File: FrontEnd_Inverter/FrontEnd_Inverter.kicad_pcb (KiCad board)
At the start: 4 copper layers, 210 x 127 mm, 75 parts, among them J1 Conn_02x20_Odd_Even, J11 CONN_02X06, P0 CONN_01X03, P10 CONN_01X02, P11 CONN_01X03, P20 CONN_01X02, P7 CONN_01X03, T1 SKiiP_13ACM12V18, U11 ACS758xCB-PFF, U12 ACS758xCB-PFF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

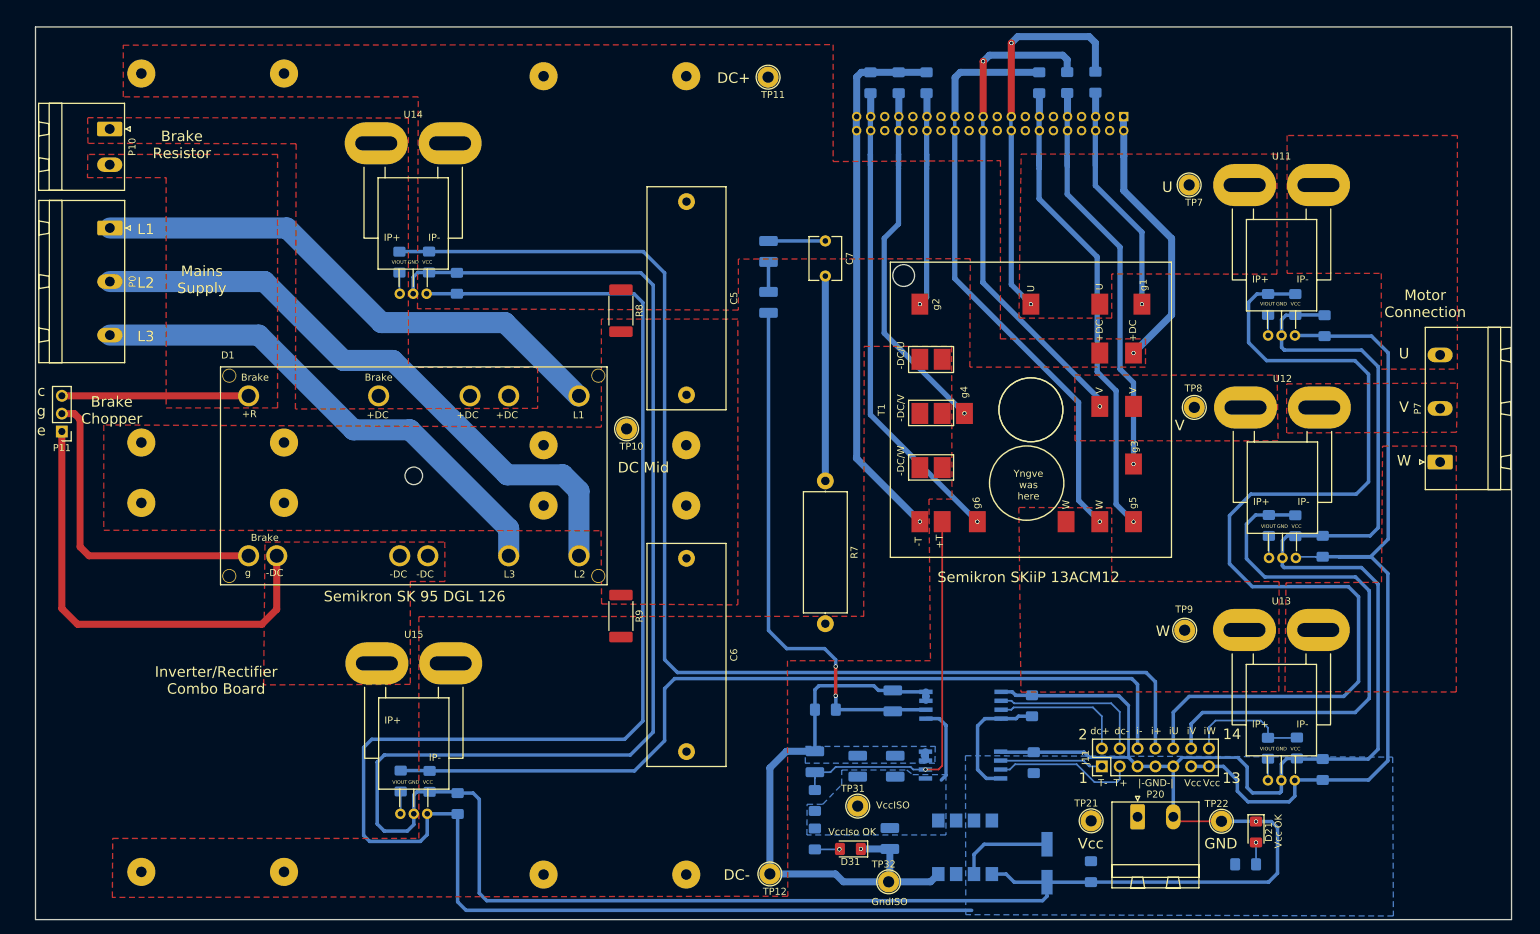
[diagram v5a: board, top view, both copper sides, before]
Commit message: Tweaking position of snubber components C7 and R7 to get closer to DC+ at inverter module T1. Work in progress.
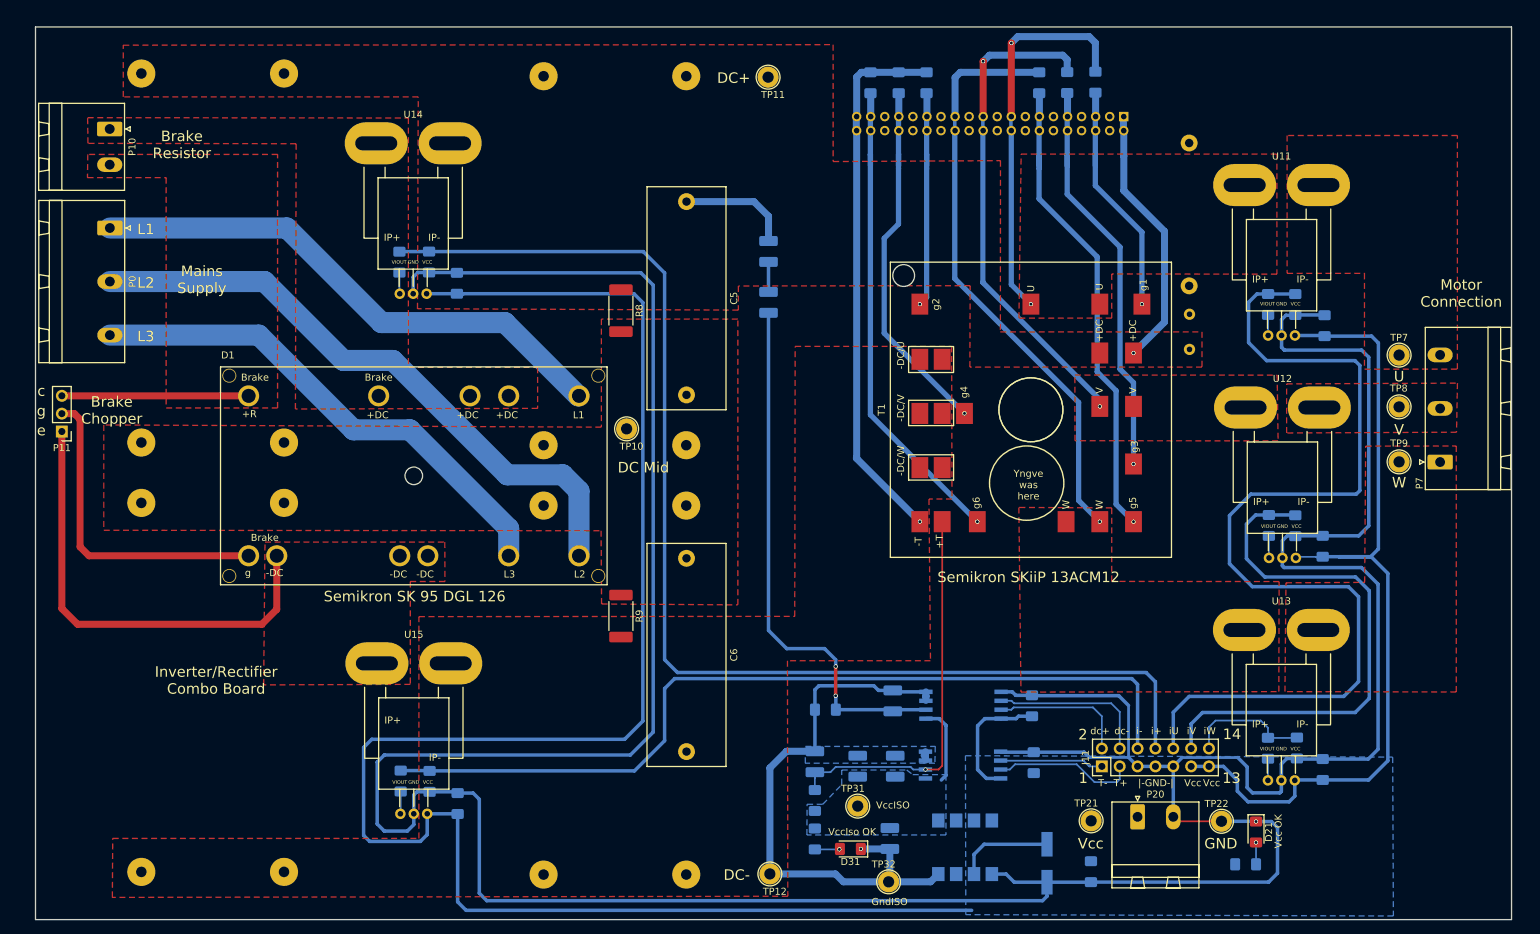
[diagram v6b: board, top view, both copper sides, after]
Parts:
- C7, R7: moved to B.Cu
- moved R7 58.7 mm to (202.1, 52.8), turned to 90 degrees
- moved C7 54.1 mm to (202.2, 61.9), turned to 90 degrees
- moved TP9 38.8 mm to (232.0, 77.9)
- moved TP7 38.4 mm to (232.0, 62.7)
- moved TP8 29.1 mm to (232.0, 70.1)
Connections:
- TP7 pad 1: U -> Net-(P7-Pad3)
- TP8 pad 1: V -> Net-(P7-Pad2)
- TP9 pad 1: W -> Net-(P7-Pad1)
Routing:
- net Net-(C7-Pad2): track 29.1 -> 0.00 mm
- net DC+: track 46.8 -> 53.9 mm
- net GND: track 532.6 -> 530.5 mm
- net VCC: track 404.0 -> 402.8 mm
- net Net-(C20-Pad1): track 141.5 -> 140.4 mm

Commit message: Finalized C7 and R7 placement. Started improving gatedriver connection with zones and vias.
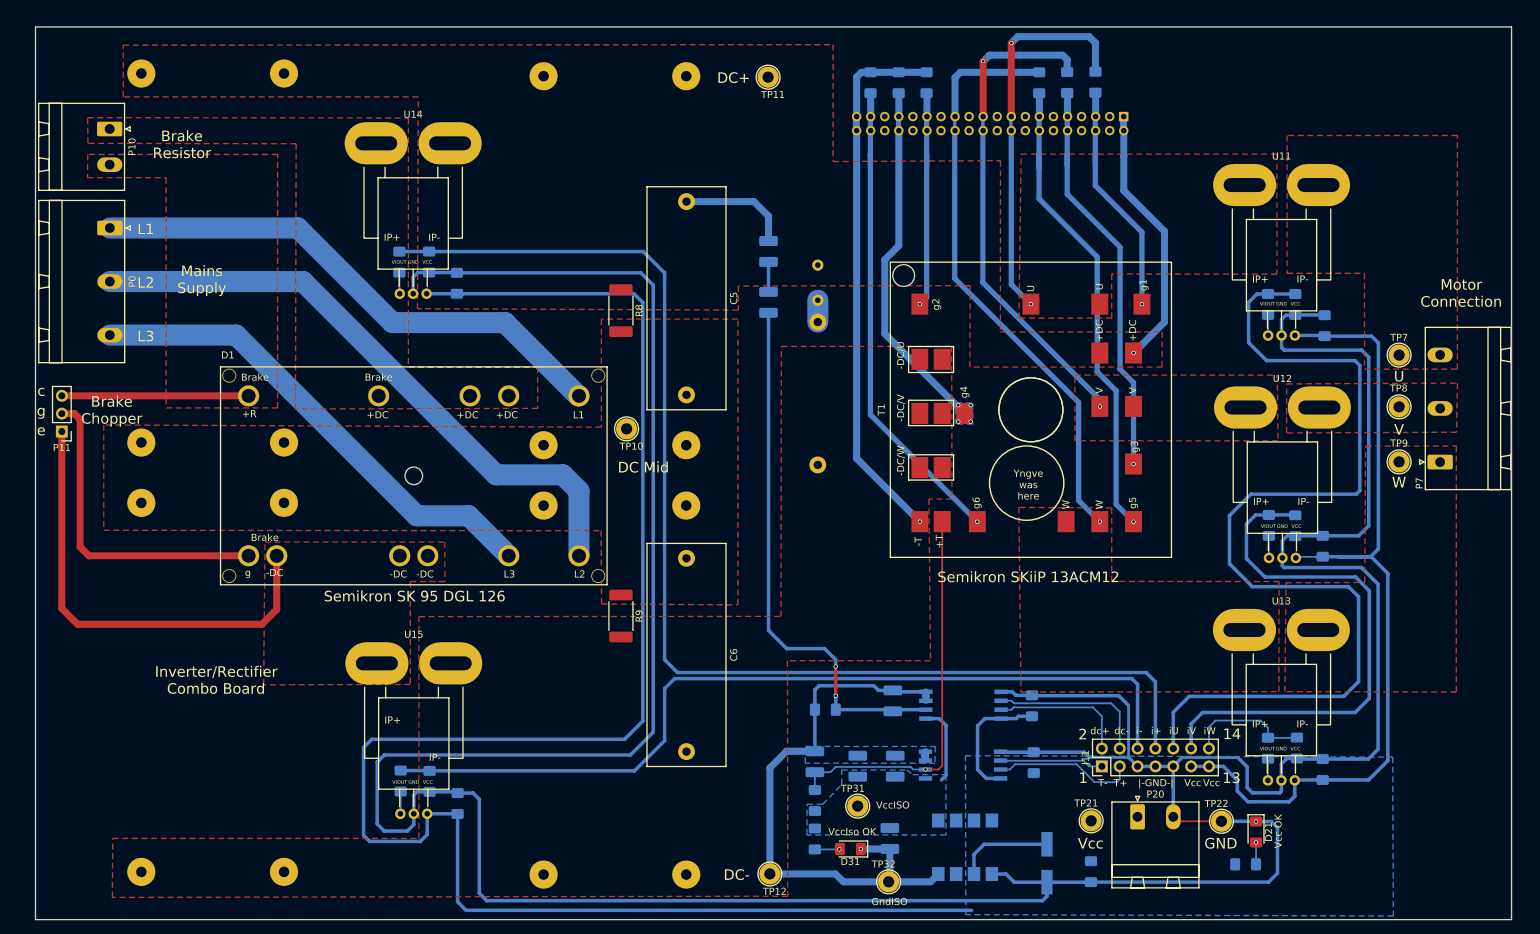
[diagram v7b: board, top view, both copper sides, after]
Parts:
- moved C7 54.2 mm to (149.3, 49.9), turned to 270 degrees
- moved R7 53.1 mm to (149.3, 58.0), turned to 270 degrees
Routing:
- net Net-(C7-Pad2): track 0.00 -> 3.10 mm
- net Net-(D1-Pad18): track 72.0 -> 69.7 mm
- net T4_g: track 52.9 -> 51.1 mm, vias 1 -> 4
- added copper zone on B.Cu, net T4_g

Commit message: Improved tracks from inverter module to pinsocket
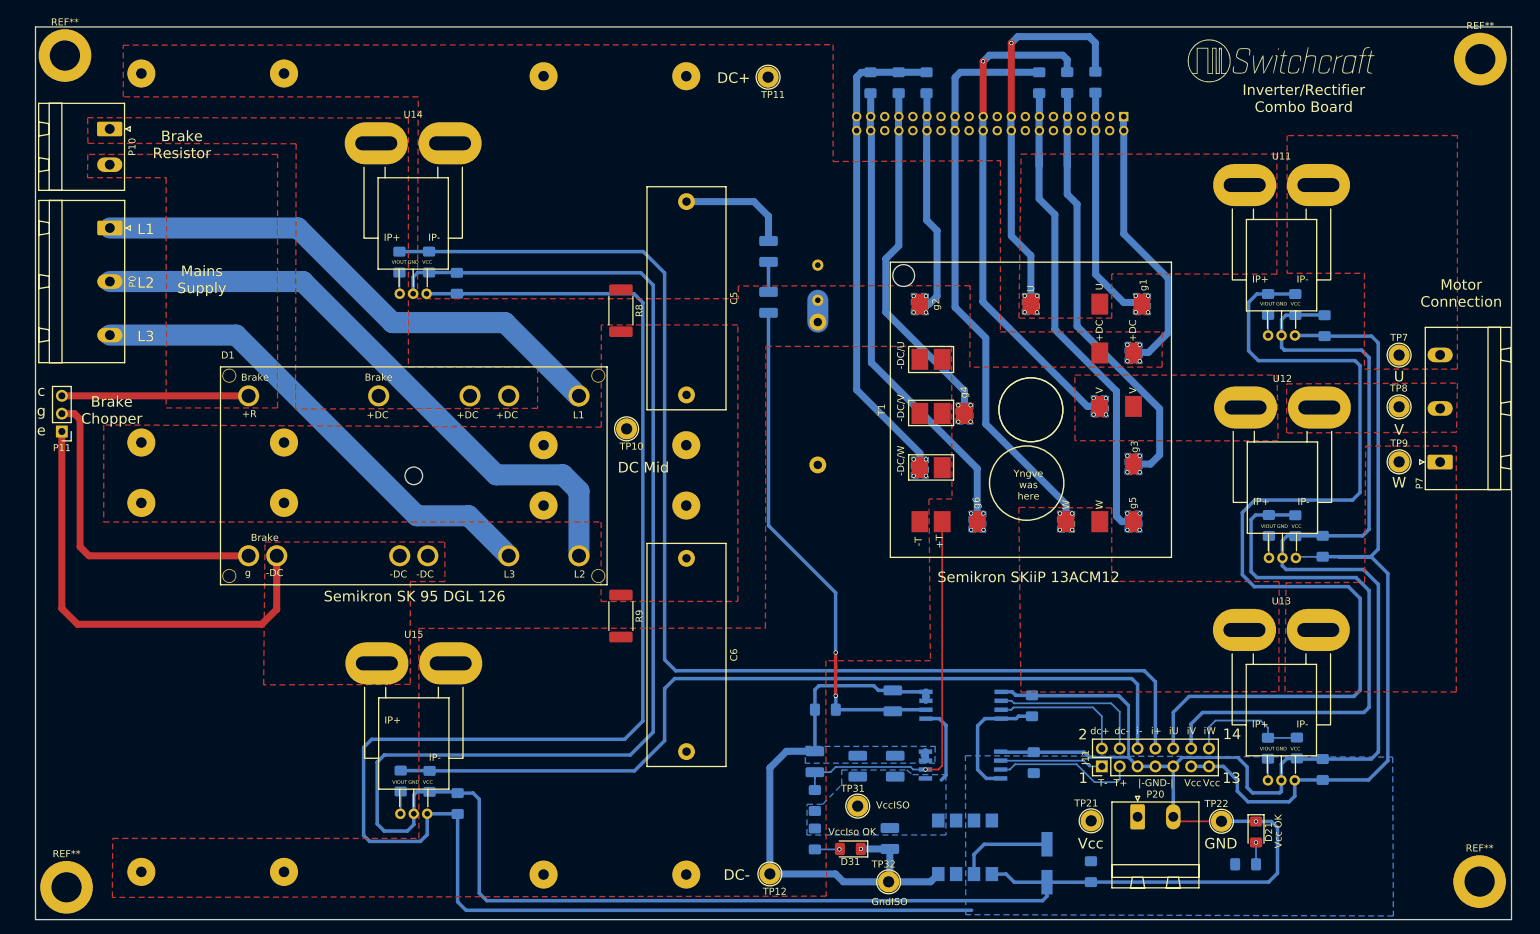
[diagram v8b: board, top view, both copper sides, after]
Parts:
- added G***: LOGO, Switchcraft:Switchcraft_logo_10px_stroke_500dpi, F.Cu at (215.2, 20.8)
- added REF**: MountingHole_4.3mm_M4_DIN965_Pad, MountingHole:MountingHole_4.3mm_M4_DIN965_Pad, F.Cu at (42.2, 20.1)
- added REF**: MountingHole_4.3mm_M4_DIN965_Pad, MountingHole:MountingHole_4.3mm_M4_DIN965_Pad, F.Cu at (42.4, 138.4)
- added REF**: MountingHole_4.3mm_M4_DIN965_Pad, MountingHole:MountingHole_4.3mm_M4_DIN965_Pad, F.Cu at (243.6, 20.6)
- added REF**: MountingHole_4.3mm_M4_DIN965_Pad, MountingHole:MountingHole_4.3mm_M4_DIN965_Pad, F.Cu at (243.5, 137.6)
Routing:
- net GND_ISO: track 161.5 -> 153.7 mm, vias 2 -> 5
- net T3_g: track 58.4 -> 62.9 mm, vias 1 -> 4
- net Net-(C51-Pad1): track 76.6 -> 73.5 mm
- net T2_g: track 32.2 -> 34.2 mm, vias 1 -> 4
- net W: track 84.0 -> 82.0 mm, vias 1 -> 4
- net T6_g: track 69.0 -> 67.4 mm, vias 1 -> 4
- net DC+: track 53.9 -> 55.4 mm, vias 1 -> 4
- net V: track 70.4 -> 71.4 mm, vias 2 -> 5
- net T5_g: track 68.3 -> 69.2 mm, vias 1 -> 4
- net Net-(C19-Pad1): track 77.6 -> 78.5 mm
- net GND: track 530.5 -> 531.2 mm
- net T1_g: track 34.6 -> 34.0 mm, vias 1 -> 4
- net Net-(C20-Pad1): track 140.4 -> 139.9 mm
- net U: vias 2 -> 5
- added copper zone on B.Cu, net DC+
- added copper zone on B.Cu, net T1_g
- added copper zone on B.Cu, net T2_g
- added copper zone on B.Cu, net T3_g
- added copper zone on B.Cu, net T5_g
- added copper zone on B.Cu, net T6_g
- added copper zone on B.Cu, net U
- added copper zone on B.Cu, net V
- added copper zone on B.Cu, net W
